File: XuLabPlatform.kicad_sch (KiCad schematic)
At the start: 0 parts

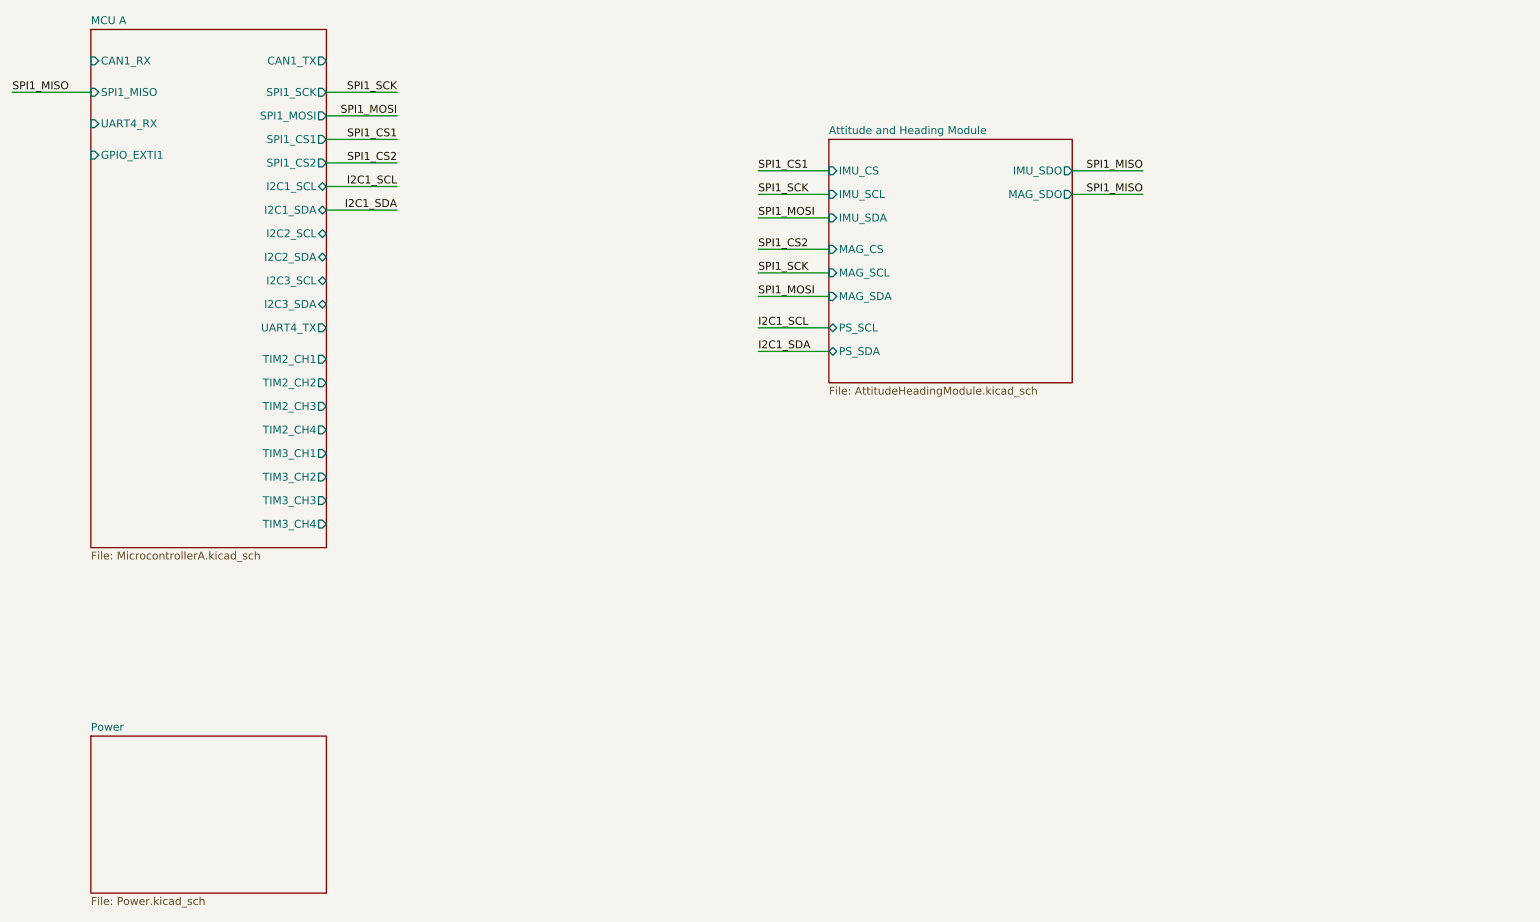
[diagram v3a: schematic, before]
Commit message: Add signal outputs for servos and change screw terminal footprints
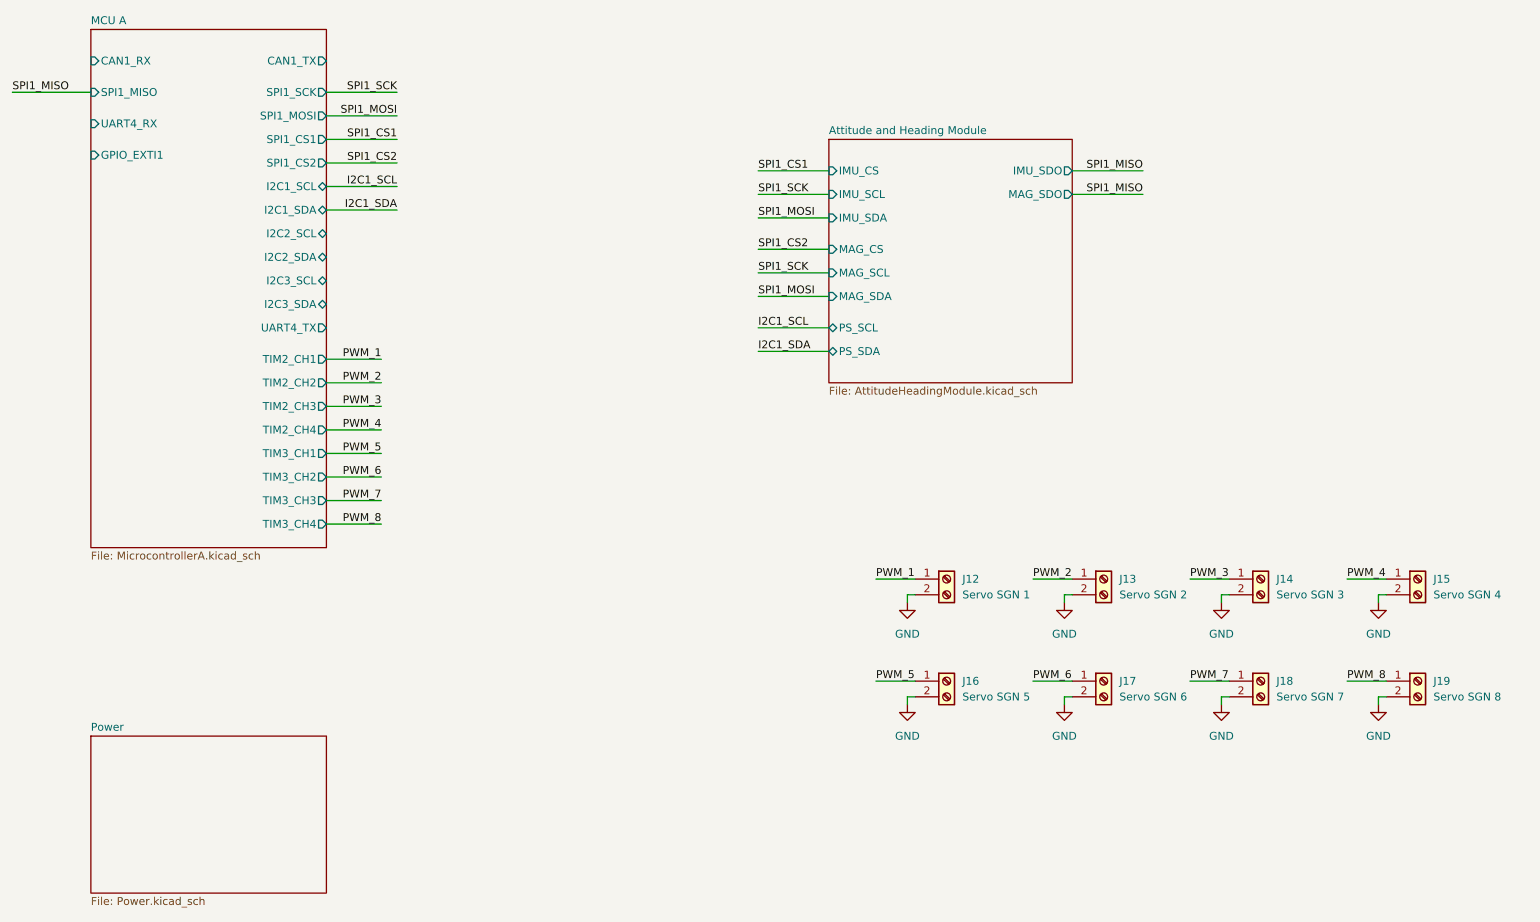
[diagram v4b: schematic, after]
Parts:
- added J12: Servo SGN 1, TerminalBlock_Phoenix:TerminalBlock_Phoenix_MKDS-1,5-2_1x02_P5.00mm_Horizontal, symbol Connector:Screw_Terminal_01x02
- added J13: Servo SGN 2, TerminalBlock_Phoenix:TerminalBlock_Phoenix_MKDS-1,5-2_1x02_P5.00mm_Horizontal, symbol Connector:Screw_Terminal_01x02
- added J14: Servo SGN 3, TerminalBlock_Phoenix:TerminalBlock_Phoenix_MKDS-1,5-2_1x02_P5.00mm_Horizontal, symbol Connector:Screw_Terminal_01x02
- added J15: Servo SGN 4, TerminalBlock_Phoenix:TerminalBlock_Phoenix_MKDS-1,5-2_1x02_P5.00mm_Horizontal, symbol Connector:Screw_Terminal_01x02
- added J16: Servo SGN 5, TerminalBlock_Phoenix:TerminalBlock_Phoenix_MKDS-1,5-2_1x02_P5.00mm_Horizontal, symbol Connector:Screw_Terminal_01x02
- added J17: Servo SGN 6, TerminalBlock_Phoenix:TerminalBlock_Phoenix_MKDS-1,5-2_1x02_P5.00mm_Horizontal, symbol Connector:Screw_Terminal_01x02
- added J18: Servo SGN 7, TerminalBlock_Phoenix:TerminalBlock_Phoenix_MKDS-1,5-2_1x02_P5.00mm_Horizontal, symbol Connector:Screw_Terminal_01x02
- added J19: Servo SGN 8, TerminalBlock_Phoenix:TerminalBlock_Phoenix_MKDS-1,5-2_1x02_P5.00mm_Horizontal, symbol Connector:Screw_Terminal_01x02
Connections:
- new net GND: J12.2 (Pin_2), J13.2 (Pin_2), J14.2 (Pin_2), J15.2 (Pin_2), J16.2 (Pin_2), J17.2 (Pin_2), J18.2 (Pin_2), J19.2 (Pin_2)
- new net PWM_1: J12.1 (Pin_1)
- new net PWM_2: J13.1 (Pin_1)
- new net PWM_3: J14.1 (Pin_1)
- new net PWM_4: J15.1 (Pin_1)
- new net PWM_5: J16.1 (Pin_1)
- new net PWM_6: J17.1 (Pin_1)
- new net PWM_7: J18.1 (Pin_1)
- new net PWM_8: J19.1 (Pin_1)

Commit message: Add thruster pin outputs
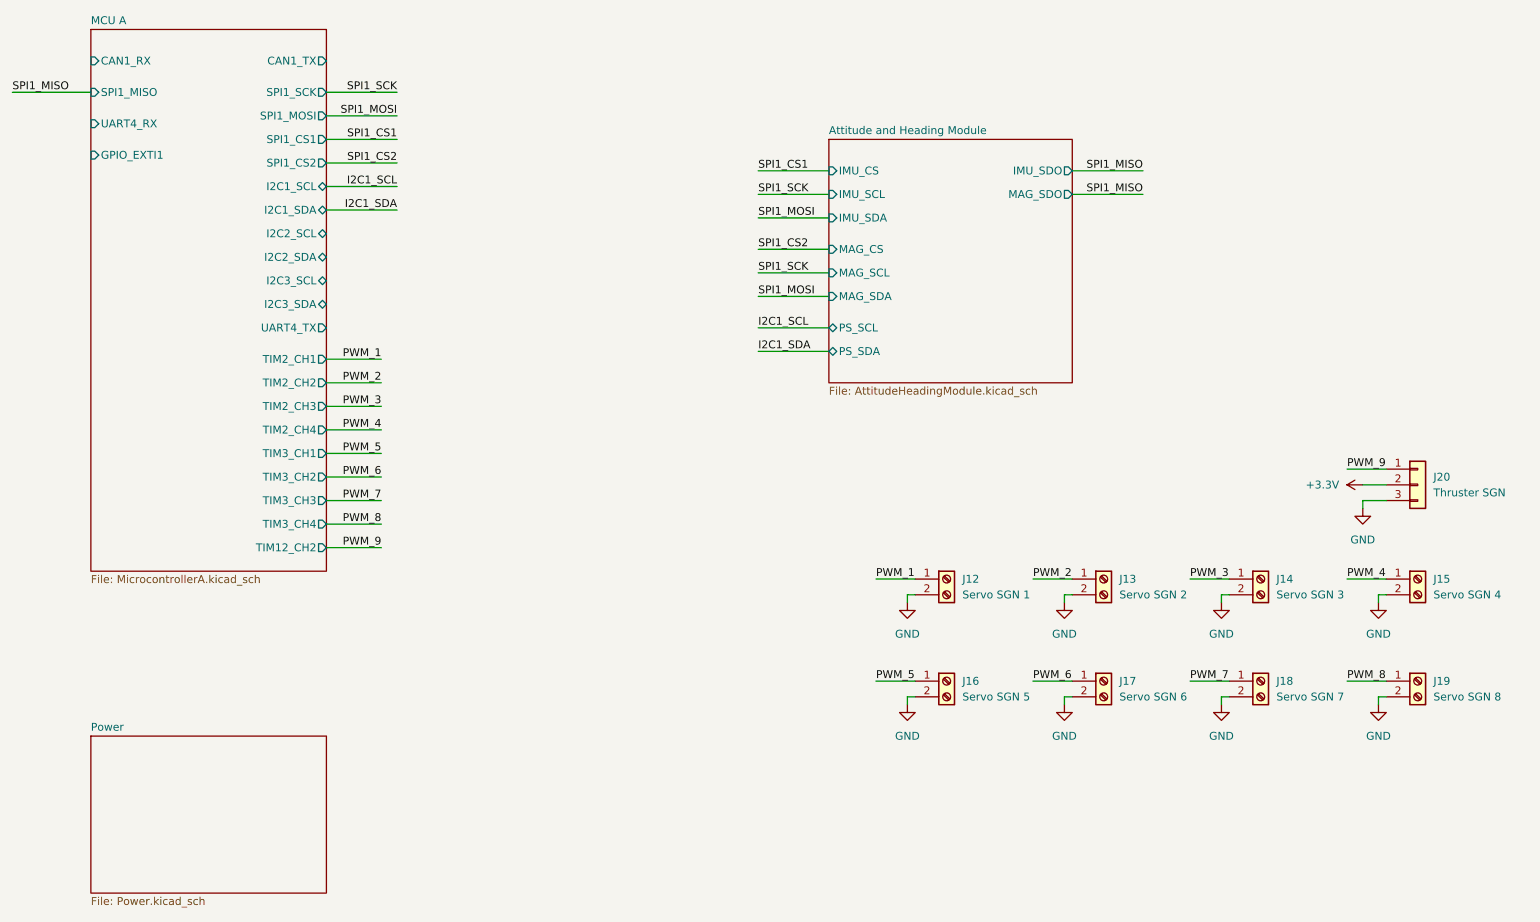
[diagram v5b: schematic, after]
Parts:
- added J20: Thruster SGN, Connector_PinHeader_2.54mm:PinHeader_1x03_P2.54mm_Vertical, symbol Connector_Generic:Conn_01x03
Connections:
- net GND: now also J20.3 (Pin_3)
- new net +3.3V: J20.2 (Pin_2)
- new net PWM_9: J20.1 (Pin_1)
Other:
- sheet MCU A ports: added TIM12_CH2; removed none

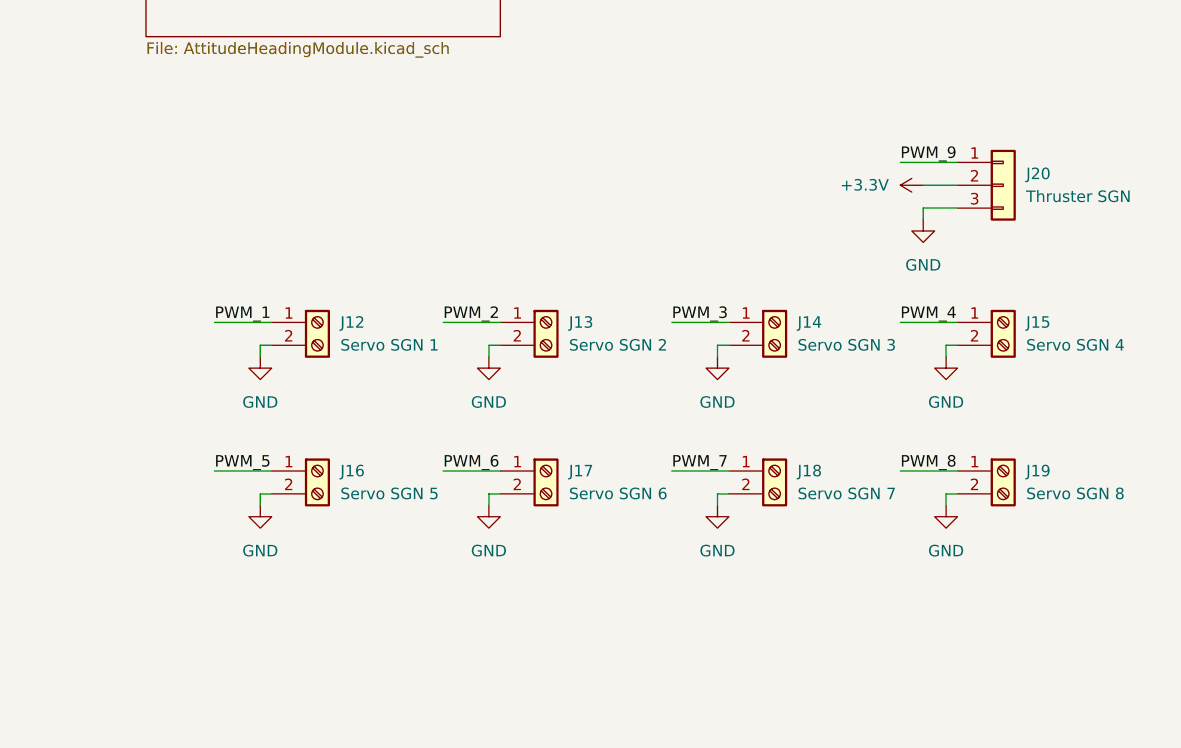
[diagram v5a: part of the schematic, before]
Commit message: Combine servo outputs to 3 pin terminal
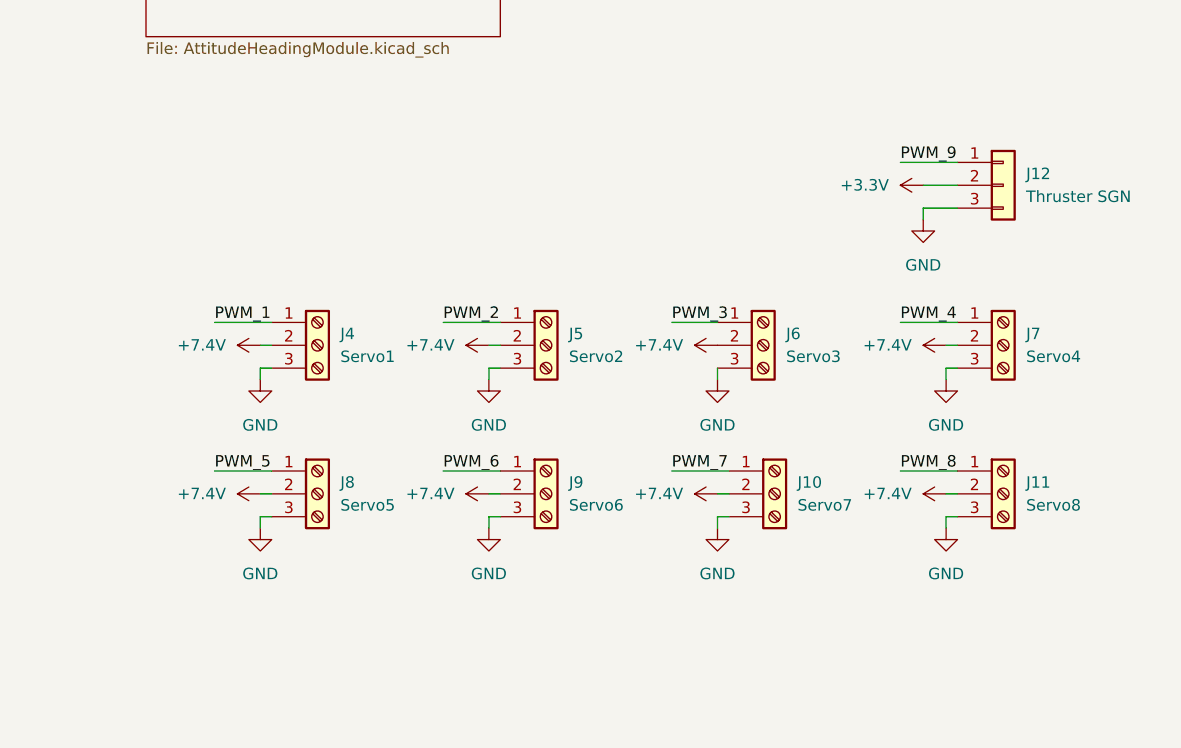
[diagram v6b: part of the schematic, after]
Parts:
- removed J12: Servo SGN 1, TerminalBlock_Phoenix:TerminalBlock_Phoenix_MKDS-1,5-2_1x02_P5.00mm_Horizontal, symbol Connector:Screw_Terminal_01x02
- removed J13: Servo SGN 2, TerminalBlock_Phoenix:TerminalBlock_Phoenix_MKDS-1,5-2_1x02_P5.00mm_Horizontal, symbol Connector:Screw_Terminal_01x02
- removed J14: Servo SGN 3, TerminalBlock_Phoenix:TerminalBlock_Phoenix_MKDS-1,5-2_1x02_P5.00mm_Horizontal, symbol Connector:Screw_Terminal_01x02
- removed J15: Servo SGN 4, TerminalBlock_Phoenix:TerminalBlock_Phoenix_MKDS-1,5-2_1x02_P5.00mm_Horizontal, symbol Connector:Screw_Terminal_01x02
- removed J16: Servo SGN 5, TerminalBlock_Phoenix:TerminalBlock_Phoenix_MKDS-1,5-2_1x02_P5.00mm_Horizontal, symbol Connector:Screw_Terminal_01x02
- removed J17: Servo SGN 6, TerminalBlock_Phoenix:TerminalBlock_Phoenix_MKDS-1,5-2_1x02_P5.00mm_Horizontal, symbol Connector:Screw_Terminal_01x02
- removed J18: Servo SGN 7, TerminalBlock_Phoenix:TerminalBlock_Phoenix_MKDS-1,5-2_1x02_P5.00mm_Horizontal, symbol Connector:Screw_Terminal_01x02
- removed J19: Servo SGN 8, TerminalBlock_Phoenix:TerminalBlock_Phoenix_MKDS-1,5-2_1x02_P5.00mm_Horizontal, symbol Connector:Screw_Terminal_01x02
- added J10: Servo7, TerminalBlock_Phoenix:TerminalBlock_Phoenix_MKDS-1,5-3-5.08_1x03_P5.08mm_Horizontal, symbol Connector:Screw_Terminal_01x03
- added J11: Servo8, TerminalBlock_Phoenix:TerminalBlock_Phoenix_MKDS-1,5-3-5.08_1x03_P5.08mm_Horizontal, symbol Connector:Screw_Terminal_01x03
- added J4: Servo1, TerminalBlock_Phoenix:TerminalBlock_Phoenix_MKDS-1,5-3-5.08_1x03_P5.08mm_Horizontal, symbol Connector:Screw_Terminal_01x03
- added J5: Servo2, TerminalBlock_Phoenix:TerminalBlock_Phoenix_MKDS-1,5-3-5.08_1x03_P5.08mm_Horizontal, symbol Connector:Screw_Terminal_01x03
- added J6: Servo3, TerminalBlock_Phoenix:TerminalBlock_Phoenix_MKDS-1,5-3-5.08_1x03_P5.08mm_Horizontal, symbol Connector:Screw_Terminal_01x03
- added J7: Servo4, TerminalBlock_Phoenix:TerminalBlock_Phoenix_MKDS-1,5-3-5.08_1x03_P5.08mm_Horizontal, symbol Connector:Screw_Terminal_01x03
- added J8: Servo5, TerminalBlock_Phoenix:TerminalBlock_Phoenix_MKDS-1,5-3-5.08_1x03_P5.08mm_Horizontal, symbol Connector:Screw_Terminal_01x03
- added J9: Servo6, TerminalBlock_Phoenix:TerminalBlock_Phoenix_MKDS-1,5-3-5.08_1x03_P5.08mm_Horizontal, symbol Connector:Screw_Terminal_01x03
- renumbered J20 to J12
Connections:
- net GND: now also J10.3 (Pin_3), J11.3 (Pin_3), J4.3 (Pin_3), J5.3 (Pin_3), J6.3 (Pin_3), J7.3 (Pin_3), J8.3 (Pin_3), J9.3 (Pin_3)
- net PWM_1: now also J4.1 (Pin_1)
- net PWM_2: now also J5.1 (Pin_1)
- net PWM_3: now also J6.1 (Pin_1)
- net PWM_4: now also J7.1 (Pin_1)
- net PWM_5: now also J8.1 (Pin_1)
- net PWM_6: now also J9.1 (Pin_1)
- net PWM_7: now also J10.1 (Pin_1)
- net PWM_8: now also J11.1 (Pin_1)
- new net +7.4V: J10.2 (Pin_2), J11.2 (Pin_2), J4.2 (Pin_2), J5.2 (Pin_2), J6.2 (Pin_2), J7.2 (Pin_2), J8.2 (Pin_2), J9.2 (Pin_2)
